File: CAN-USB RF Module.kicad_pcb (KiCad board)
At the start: 4 copper layers, 115 parts, among them IC1 ESDALC6V1W5, J1 USB JMPR, J2 USB_B_Micro, J3 Conn_Coaxial, J4 Conn_01x02_Socket, J5 Conn_02x05_Top_Bottom, J6 Fuel Cell Connector, Q1 NMOS, Q2 NMOS, SW1 RESET, SW2 BOOT0, SW3 GPBTN, SW4 GPSW, U1 STM32L442KCU6, U4 FT234XD-R, U5 SX1276IMLTRT, U6 P4259-63, U7 MCP2542WFDxMF (CAN), U8 MAX14572, U9 TLV76601QWDRBRQ1, Y1 32MHz

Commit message: Done design
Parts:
- removed CR1: ESDCAN03-2BWY, footprints:SOT323-3L_STM
- removed J4: Conn_01x02_Socket, Connector_PinHeader_2.54mm:PinHeader_1x02_P2.54mm_Vertical
- removed R25, R29: 10k, Resistor_SMD:R_0402_1005Metric
- removed SW3: GPBTN, footprints:SMD_025816_WRE
- removed SW4: GPSW, Button_Switch_SMD:SW_SPDT_PCM12
- removed U7: MCP2542WFDxMF (CAN), Package_DFN_QFN:DFN-8-1EP_3x3mm_P0.65mm_EP1.55x2.4mm
- added C52: 1u, Capacitor_SMD:C_0603_1608Metric, F.Cu at (112.0, 105.7)
- added C53: 1u, Capacitor_SMD:C_0603_1608Metric, F.Cu at (116.7, 105.7)
- added C54: 10u, Capacitor_SMD:C_0603_1608Metric, F.Cu at (116.7, 104.1)
- added C55: 1u, Capacitor_SMD:C_0402_1005Metric, F.Cu at (149.7, 114.8)
- added C56: 22u, Capacitor_SMD:C_0603_1608Metric, F.Cu at (146.4, 115.1)
- added C57: 1u, Capacitor_SMD:C_0402_1005Metric, F.Cu at (147.7, 114.8)
- added C58: 1u, Capacitor_SMD:C_0402_1005Metric, F.Cu at (148.7, 114.8)
- added D11: BLUE, LED_SMD:LED_0603_1608Metric, F.Cu at (121.7, 101.5)
- added J7: Conn_01x09_Socket, Connector_Dsub:DSUB-9_Female_Horizontal_P2.77x2.84mm_EdgePinOffset7.70mm_Housed_MountingHolesOffset9.12mm, F.Cu at (138.8, 79.7)
- added R30: 600R, Resistor_SMD:R_0603_1608Metric, F.Cu at (121.7, 98.4)
- added U2: LP38690DTX, Package_TO_SOT_SMD:TO-252-3_TabPin2, F.Cu at (113.5, 112.9)
- added U3: MCP2542FDxMF, Package_DFN_QFN:DFN-8-1EP_3x3mm_P0.65mm_EP1.55x2.4mm, F.Cu at (138.7, 87.9)
- J2: footprint Connector_USB:USB_Micro-B_Amphenol_10118194_Horizontal -> footprints:USB_Micro-B_Amphenol_10118194_Horizontal; moved to F.Cu
- J3: footprint Connector_Coaxial:SMA_Amphenol_132289_EdgeMount -> footprints:TAOGLAS_EMPCB.SMAFSTJ.B.HT
- J6: footprint Connector_Molex:Molex_Micro-Fit_3.0_43045-0621_2x03-1MP_P3.00mm_Horizontal -> footprints:Molex_Micro-Fit_3.0_43045-0621_2x03-1MP_P3.00mm_Horizontal
- RV1: footprint Potentiometer_THT:Potentiometer_Bourns_3386P_Vertical -> footprints:Potentiometer_Bourns_3386P_Vertical
- moved J6 120.4 mm to (104.9, 81.2)
- moved D1 117.1 mm to (189.1, 76.1)
- moved J5 112.9 mm to (183.6, 75.4), turned to -90 degrees
- moved J2 112.0 mm to (122.2, 73.9), turned to 180 degrees
- moved C40 111.6 mm to (141.5, 86.2)
- moved JP2 108.7 mm to (113.2, 84.1), turned to -90 degrees
- moved IC1 107.5 mm to (169.8, 76.8), turned to 180 degrees
- moved C13 106.5 mm to (125.4, 80.1), turned to 180 degrees
- moved R11 104.6 mm to (111.2, 86.9), turned to 180 degrees
- moved C39 104.0 mm to (138.9, 90.9), turned to 90 degrees
- moved R22 102.4 mm to (109.5, 88.4), turned to 180 degrees
- moved D5 101.4 mm to (114.1, 89.7), turned to -90 degrees
- moved D3 100.1 mm to (122.6, 80.0), turned to 0 degrees
- moved R10 99.6 mm to (110.7, 90.4), turned to 180 degrees
- moved R19 97.6 mm to (113.3, 91.9), turned to 0 degrees
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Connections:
- net Net-(U5-PA_BOOST) renamed /LoRa Tranciever/RFO_HF
- U1 pad 2: Net-(U1-PC14) -> /DIO5
- U1 pad 25: Net-(U1-PA15) -> /DIO4
- U5 pad 12: /DIO3 -> /DIO4
- U5 pad 13: /DIO3 -> /DIO5
- U8 pad 15: (no net) -> GND
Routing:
- net +3V3: track 25.3 -> 318.9 mm, vias 5 -> 20
- net /SW_RXTX: track 0.00 -> 77.1 mm, vias 0 -> 4
- net +5V: track 3.97 -> 69.4 mm, vias 0 -> 4
- net /DEBUG_SWDIO: track 18.5 -> 68.7 mm
- net /DEBUG_SWCLK: track 22.4 -> 66.9 mm, vias 2 -> 4
- net /DEBUG_SWO: track 23.9 -> 63.9 mm
- net VBUS_UP: track 52.4 -> 14.6 mm, vias 3 -> 1
- net /DIO5: track 0.00 -> 36.4 mm, vias 0 -> 4
- net /LoRa Tranciever/RXTX_SX: track 0.00 -> 32.0 mm, vias 0 -> 2
- net Net-(U1-PA15): track 31.0 -> 0.00 mm, vias 2 -> 0
- net /DIO3: track 0.00 -> 30.4 mm, vias 0 -> 2
- net /SPI1_NSS: track 0.00 -> 28.6 mm
- net /CAN_RX: track 43.0 -> 15.0 mm
- net /DIO2: track 0.00 -> 27.1 mm, vias 0 -> 2
- net /SX_RESET: track 0.00 -> 26.1 mm, vias 0 -> 2
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- added copper zone on F.Cu, net +12V
- added copper zone on In2.Cu, net +5V
- added copper zone on F.Cu, net /Power Regulator/12V
- added copper zone on B.Cu, net GND
- added copper zone on F.Cu, net GND
- added copper zone on In1.Cu, net GND
- removed copper zone on F.Cu, net +5V
- removed copper zone on In2.Cu, net VBUS_UP
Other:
- board outline added: 95 x 47.2 mm
- board text added: "Horizontal Top Layer Vertical Bottom layer"
- board text added: "RESET"
- board text added: "USB RX/TX"
- board text removed: "RX/TX"

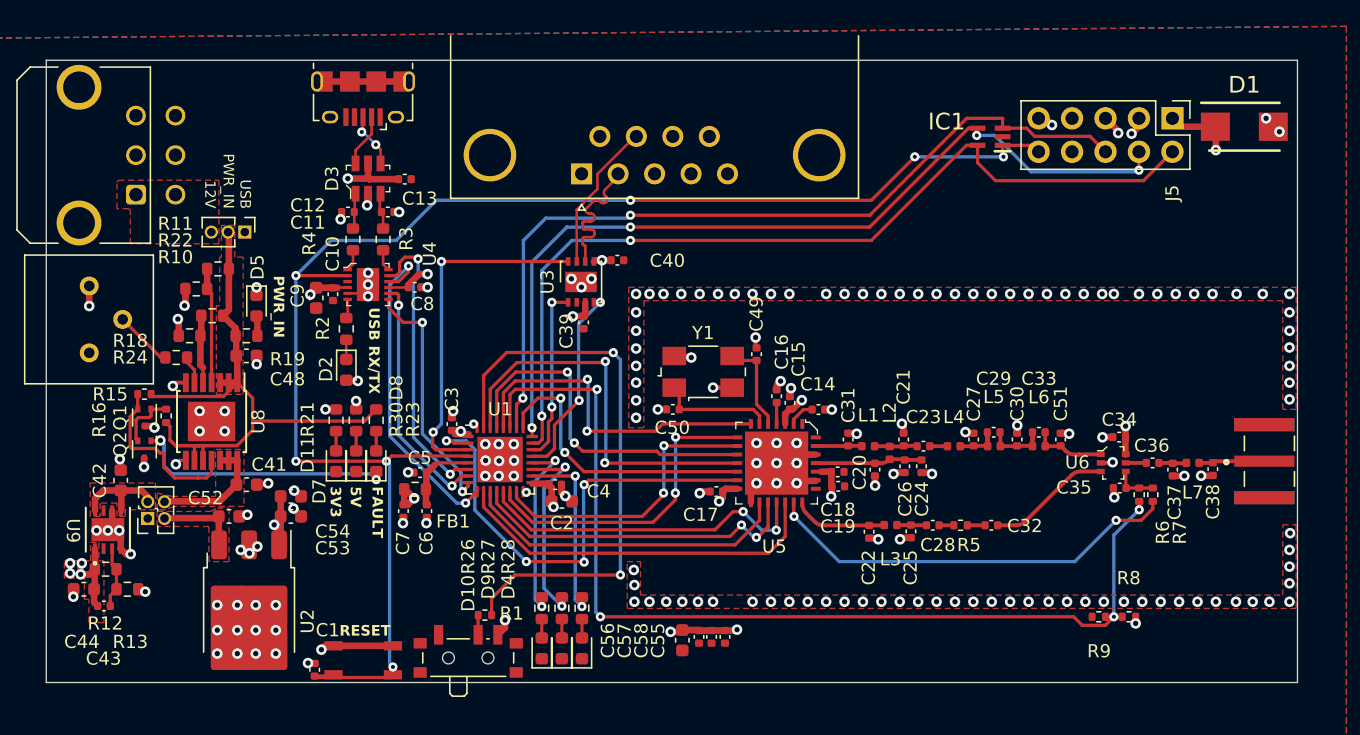
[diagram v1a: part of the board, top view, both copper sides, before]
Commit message: Added stiching vias
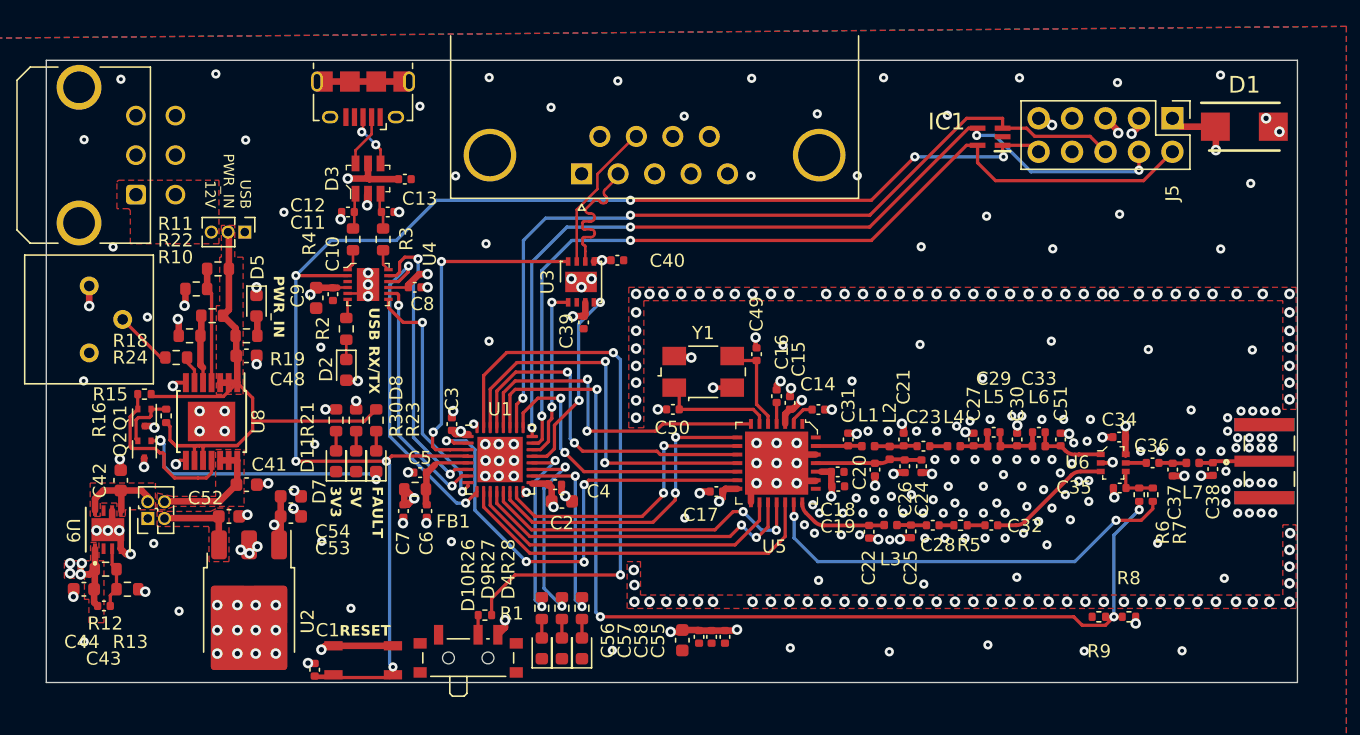
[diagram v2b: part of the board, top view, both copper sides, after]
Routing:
- net /LoRa Tranciever/RXTX_SX: track 32.0 -> 32.9 mm
- net +3V3: track 318.9 -> 319.7 mm
- net GND: vias 194 -> 349

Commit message: a
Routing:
- net VBUS_UP: track 14.6 -> 24.5 mm, vias 1 -> 3
- net /SPI1_NSS: track 28.6 -> 29.8 mm
- net /SPI1_SCK: track 24.9 -> 25.8 mm
- net /SPI1_MISO: track 25.5 -> 26.2 mm
- net /DIO5: track 36.4 -> 37.0 mm
- net GND: vias 349 -> 389
- added copper zone on In2.Cu, net VBUS_UP

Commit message: Done
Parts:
- removed C52, C53: 1u, Capacitor_SMD:C_0603_1608Metric
- removed R12: 500k, Resistor_SMD:R_0603_1608Metric
- removed R13: 160k, Resistor_SMD:R_0603_1608Metric
- removed U9: TLV76601QWDRBRQ1, footprints:TLV76601QWDRBRQ1_TEX
- added U7: AZ1117-3.3, Package_TO_SOT_SMD:SOT-223-3_TabPin2, F.Cu at (107.3, 112.4)
- C42: value 1u -> 10u
- C43: value 10p -> 10u; footprint Capacitor_SMD:C_0402_1005Metric -> Capacitor_SMD:C_0603_1608Metric
- C44: value 2u2 -> 22u
- C54: value 10u -> 22u
- J1: footprint Connector_PinHeader_1.27mm:PinHeader_2x02_P1.27mm_Vertical -> Connector_PinHeader_2.54mm:PinHeader_2x02_P2.54mm_Vertical
- JP2: footprint Connector_PinHeader_1.27mm:PinHeader_1x03_P1.27mm_Vertical -> Connector_PinHeader_2.54mm:PinHeader_1x03_P2.54mm_Vertical
- U2: value LP38690DTX -> AZ1117-5.0; footprint Package_TO_SOT_SMD:TO-252-3_TabPin2 -> Package_TO_SOT_SMD:SOT-223-3_TabPin2
- moved C42 14.0 mm to (104.9, 116.8), turned to 0 degrees
- moved C43 13.6 mm to (114.0, 105.2)
- moved C54 11.7 mm to (116.3, 115.8)
- moved U2 3.24 mm to (115.7, 110.5)
- moved J1 1.86 mm to (107.4, 106.9)
- moved JP2 1.35 mm to (114.5, 84.3)
- moved R22 1.32 mm to (110.7, 88.9)
- moved C44 1.16 mm to (102.1, 111.5), turned to 90 degrees
- moved R10 1.03 mm to (111.8, 90.4)
- moved R18 0.96 mm to (110.0, 91.9)
- moved R11 0.77 mm to (111.8, 87.4)
- moved C49 0.17 mm to (151.9, 93.3)
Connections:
- C43 pad 1: +3V3 -> /Power Regulator/12V
- C43 pad 2: /Power Regulator/FB -> GND
- U2 pad 1: +5V -> GND
- U2 pad 2: GND -> +5V
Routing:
- net GND: track 69.5 -> 57.4 mm, vias 389 -> 361
- net +3V3: track 319.7 -> 309.6 mm, vias 20 -> 19
- net /Power Regulator/5V: track 7.30 -> 15.7 mm, vias 0 -> 1
- net /Power Regulator/FB: track 4.68 -> 0.00 mm
- net +5V: track 69.4 -> 73.8 mm
- net /CAN Tranciever/CD-: track 11.3 -> 7.69 mm
- net /Power Regulator/FUSE_OUT: track 9.14 -> 6.23 mm
- net VBUS_UP: track 24.5 -> 26.1 mm, vias 3 -> 2
- net Net-(R24-Pad2): track 4.44 -> 5.58 mm
- net /DEBUG_SWO: track 64.0 -> 63.4 mm
- net /Power Regulator/FUSE_IN: track 50.3 -> 49.7 mm
- added copper zone on In2.Cu, net +3V3
- added copper zone on F.Cu, net +5V
- added copper zone on In2.Cu, net /Power Regulator/5V
- removed copper zone on F.Cu, net +12V
- removed copper zone on In2.Cu, net +5V
- removed copper zone on F.Cu, net /Power Regulator/5V

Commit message: Added logo and assigned parts
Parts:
- removed the Q1 at (105.6, 98.2)
- removed the R16 at (107.2, 98.0)
- added G***: LOGO, LOGO, B.Cu at (178.9, 116.5)
- added H1: MountingHole, MountingHole:MountingHole_2.2mm_M2, F.Cu at (189.7, 73.9)
- added H2: MountingHole, MountingHole:MountingHole_2.2mm_M2, F.Cu at (189.9, 115.6)
- added H3: MountingHole, MountingHole:MountingHole_2.2mm_M2, F.Cu at (114.6, 74.2)
- added H4: MountingHole, MountingHole:MountingHole_2.2mm_M2, F.Cu at (114.7, 115.6)
- added U9: Common Cathode SBD, Package_TO_SOT_SMD:SOT-23, F.Cu at (116.5, 79.5)
- C2: footprint Capacitor_SMD:C_0603_1608Metric -> Capacitor_SMD:C_0805_2012Metric
- D10: renamed from D2; value AMBER RX/TX -> AMBER
- SW2: renamed from SW1; footprint footprints:SMD_025816_WRE -> Button_Switch_SMD:SW_SPST_PTS810
- Y1: footprint Crystal:Crystal_SMD_0603-4Pin_6.0x3.5mm -> Crystal:Crystal_SMD_2016-4Pin_2.0x1.6mm
- moved C13 10.0 mm to (123.4, 108.6), turned to -90 degrees
- moved Q1 9.00 mm to (114.6, 101.3)
- moved R15 8.46 mm to (114.0, 96.5), turned to -90 degrees
- moved C11 6.82 mm to (112.9, 109.9), turned to -90 degrees
- moved D4 4.42 mm to (187.7, 80.3), turned to -90 degrees
- moved C21 3.26 mm to (149.0, 97.7)
- moved U4 2.74 mm to (118.2, 109.3), turned to 180 degrees
- moved Y1 2.43 mm to (150.2, 95.8)
- moved C20 1.55 mm to (152.1, 94.9)
- moved C2 0.97 mm to (138.2, 104.9)
- moved SW2 0.25 mm to (122.2, 116.3)
- moved C1 0.13 mm to (118.6, 117.2)
- renumbered C42 to C10, C54 to C11, C41 to C12, C43 to C13, C8 to C14, C9 to C15, C10 to C16, C11 to C17, C12 to C18, C13 to C19, C49 to C20, C50 to C21, C14 to C22, C15 to C23, C16 to C24, C17 to C25, C18 to C26, C19 to C27, C31 to C28, C20 to C29, C21 to C30, C23 to C31, C22 to C32, C24 to C33, C26 to C34, C25 to C35, C27 to C36, C55 to C37, C28 to C38, C29 to C39, C30 to C40, C33 to C41, C32 to C42, C51 to C43, C56 to C44, C34 to C45, C57 to C46, C35 to C47, C58 to C48, C36 to C49, C37 to C50, C38 to C51, C39 to C52, C40 to C53, C44 to C8, C48 to C9, D10 to D1, D3 to D11, D9 to D2, D4 to D3, D1 to D4, D7 to D6, D11 to D7, D8 to D9, J5 to J1, J1 to J2, J6 to J3, J2 to J4, J3 to J5, J7 to J6, JP2 to JP1, Q2 to Q1, R18 to R10, R22 to R12, R24 to R13, R30 to R14, R23 to R16, R2 to R17, R3 to R18, R4 to R19, R1 to R2, R5 to R20, R6 to R21, R7 to R22, R8 to R23, R9 to R24, R26 to R4, R27 to R5, R28 to R6, R19 to R7, R21 to R8, R10 to R9, SW2 to SW3, U7 to U2, U8 to U3, U2 to U4, U4 to U5, U5 to U6, U6 to U7, U3 to U8
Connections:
- J3 pad 3: unconnected-(J6-Pin_3-Pad3) (its old number) -> /Power Regulator/5V_UP
- J3 pad 6: unconnected-(J6-Pin_6-Pad6) (its old number) -> /Power Regulator/5V_UP
- Q1 pad 2: Net-(Q1-D) -> /Power Regulator/~{FLAG}
- R15 pad 1: /Power Regulator/FUSE_IN -> Net-(R15-Pad1)
- R16 pad 1: /Power Regulator/FUSE_IN -> Net-(R15-Pad1)
- SW2 pad 2: GND -> /NRST
- U3 pad 10: /Power Regulator/FUSE_IN -> GND
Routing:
- net /Power Regulator/FUSE_IN: track 49.7 -> 22.3 mm
- net Net-(R15-Pad1): track 0.00 -> 26.9 mm
- net /Power Regulator/5V_UP: track 0.00 -> 12.4 mm
- net Net-(D9-K): track 19.9 -> 10.1 mm, vias 2 -> 0
- net VBUS_UP: track 26.1 -> 35.4 mm
- net /Power Regulator/12V: track 5.97 -> 14.5 mm
- net Net-(Q1-D): track 4.59 -> 0.00 mm
- net /Power Regulator/~{FLAG}: track 13.0 -> 8.39 mm
- net Net-(U6-XTB): track 8.73 -> 5.04 mm
- net +3V3: track 309.6 -> 307.2 mm
- net Net-(U6-XTA): track 7.06 -> 5.00 mm
- net /NRST: track 116.4 -> 114.7 mm
- net /DIO1: track 22.3 -> 23.5 mm
- net /SPI1_SCK: track 25.8 -> 26.8 mm
- net /DIO0: track 24.4 -> 25.3 mm
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- added copper zone on F.Cu, net +12V
- removed copper zone on In2.Cu, net +3V3
- removed copper zone on F.Cu, net /Power Regulator/12V
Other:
- board text added: "Telemetry Module Rev 1.0"
- board text added: "~{FAULT}"
- board text removed: "EcoCar Telemetry Module Rev 1.0"
- board text removed: "FAULT"

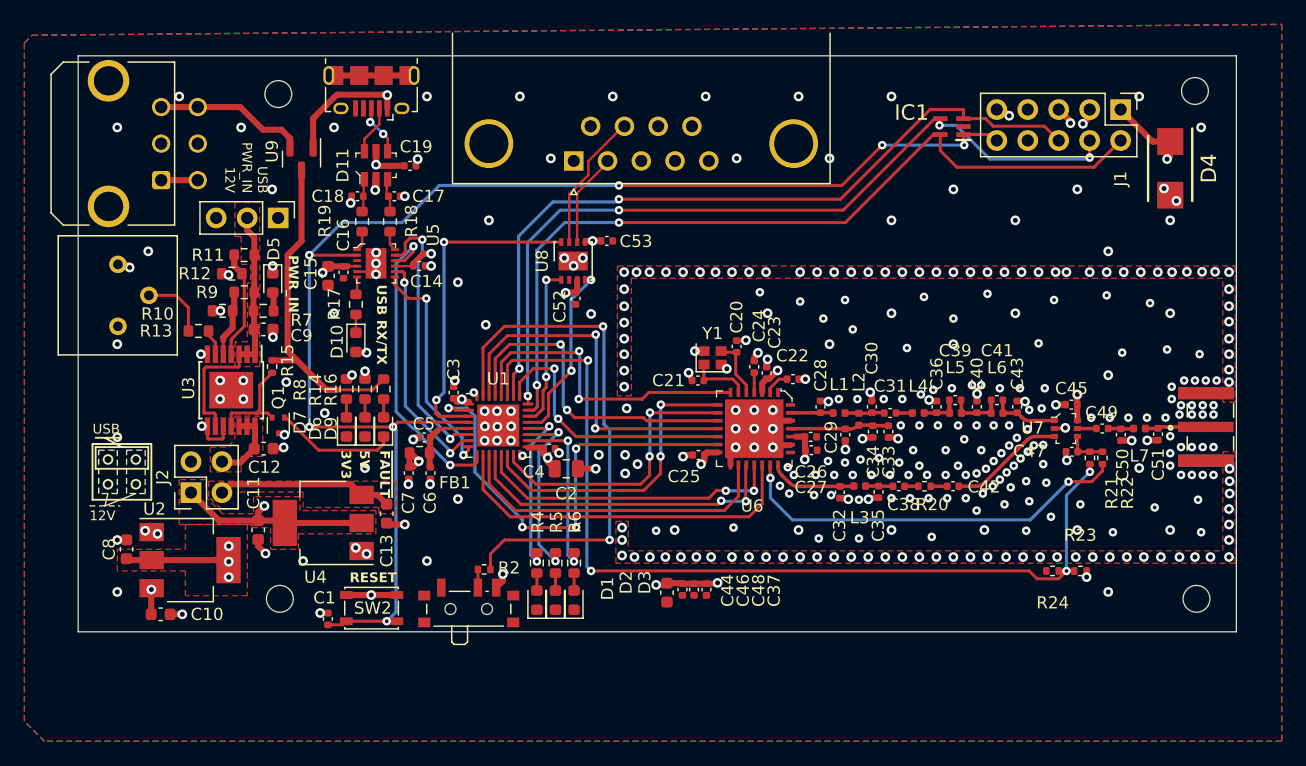
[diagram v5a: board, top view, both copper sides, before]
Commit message: Ready to order added all part numbers
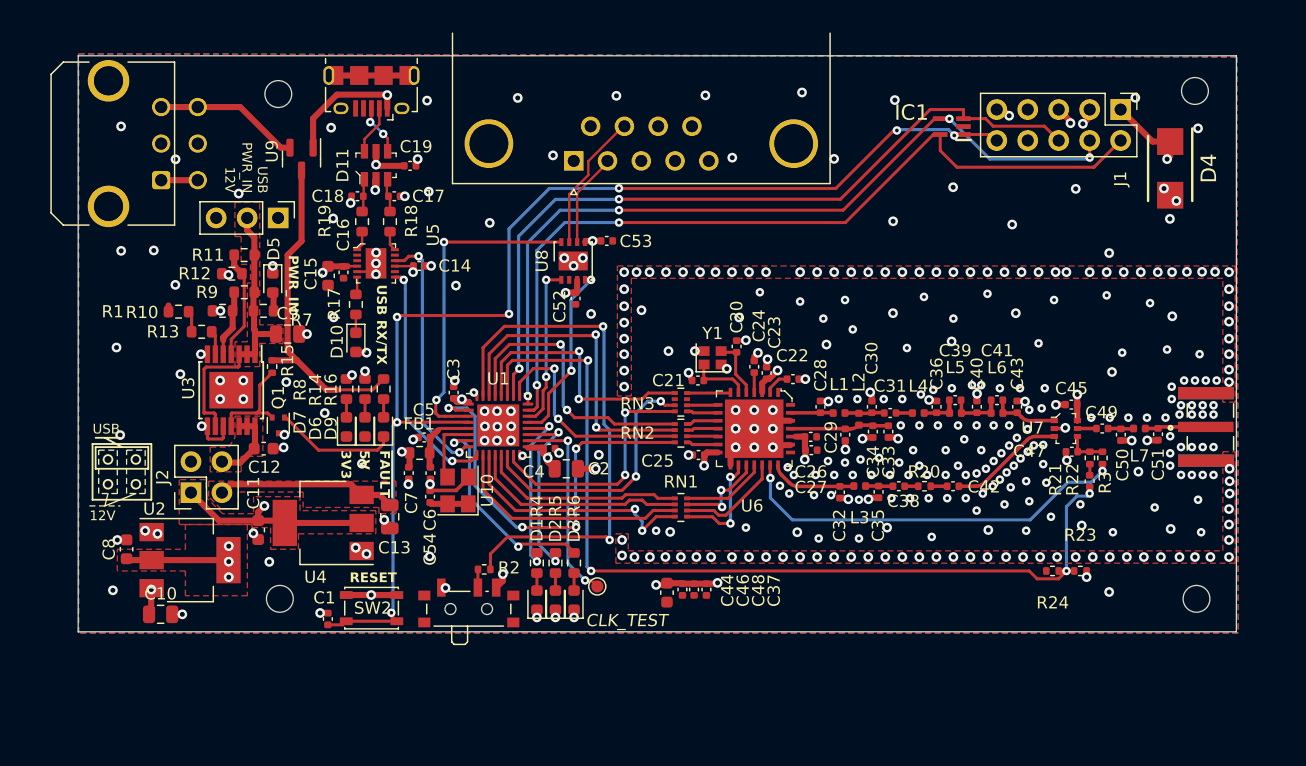
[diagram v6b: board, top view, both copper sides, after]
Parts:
- removed RV1: SETI, footprints:Potentiometer_Bourns_3386P_Vertical
- added C54: u1, Capacitor_SMD:C_0402_1005Metric, F.Cu at (127.0, 107.2)
- added R1: 1k5, Resistor_SMD:R_0603_1608Metric, F.Cu at (106.4, 92.0)
- added R3: 100R, Capacitor_SMD:C_0402_1005Metric, F.Cu at (181.1, 105.9)
- added RN1: 100R, Resistor_SMD:R_Array_Concave_4x0402, F.Cu at (147.6, 108.1)
- added RN2: 100R, Resistor_SMD:R_Array_Concave_4x0402, F.Cu at (147.6, 102.0)
- added RN3: 100R, Resistor_SMD:R_Array_Concave_4x0402, F.Cu at (147.6, 99.4)
- added TP1: CLK_TEST, TestPoint:TestPoint_Pad_D1.0mm, F.Cu at (140.7, 114.6)
- added U10: 8MHz, Crystal:Crystal_SMD_3225-4Pin_3.2x2.5mm, F.Cu at (129.3, 106.7)
- C10, C13, C9: footprint Capacitor_SMD:C_0603_1608Metric -> Capacitor_SMD:C_0805_2012Metric
- R4, R5, R6: value 10k -> 110R
- moved G*** 31.2 mm to (186.1, 86.1)
- moved C9 2.01 mm to (115.3, 93.9)
- moved C13 0.36 mm to (123.7, 108.8)
- moved R13 0.27 mm to (108.3, 93.7)
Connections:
- R21 pad 2: /SW_RXTX -> /LoRa Tranciever/RXTX_EXT
- R23 pad 1: /SW_RXTX -> /LoRa Tranciever/RXTX_EXT
- R24 pad 2: /SW_RXTX -> /LoRa Tranciever/RXTX_EXT
- R6 pad 2: Net-(U1-PA8) -> Net-(U1-PA1)
- U1 pad 6: /UART2_USB_CTS -> /XCLK
- U1 pad 7: /UART2_USB_RTS -> Net-(U1-PA1)
- U5 pad 10: /UART2_USB_RX -> /UART2_USB_TX
- U5 pad 11: /UART2_USB_CTS -> /USB Interface/CTS
- U5 pad 2: /NRST -> /USB Interface/RESET
- U5 pad 7: /UART2_USB_TX -> /UART2_USB_RX
- U5 pad 8: /UART2_USB_RTS -> /USB Interface/RTS
- U6 pad 10: /DIO2 -> /LoRa Tranciever/DIO2
- U6 pad 11: /DIO3 -> /LoRa Tranciever/DIO3
- U6 pad 12: /DIO4 -> /LoRa Tranciever/DIO4
- U6 pad 13: /DIO5 -> /LoRa Tranciever/DIO5
- U6 pad 16: /SPI1_SCK -> /LoRa Tranciever/SCK_RTSN
- U6 pad 17: /SPI1_MISO -> /LoRa Tranciever/MISO_TX
- U6 pad 18: /SPI1_MOSI -> /LoRa Tranciever/MOSI_RX
- U6 pad 19: /SPI1_NSS -> /LoRa Tranciever/NSS_CTS
- U6 pad 7: /SX_RESET -> /LoRa Tranciever/SX1276_NRESET
- U6 pad 8: /DIO0 -> /LoRa Tranciever/DIO0
- U6 pad 9: /DIO1 -> /LoRa Tranciever/DIO1
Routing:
- net /UART2_USB_CTS: track 22.6 -> 0.00 mm, vias 2 -> 0
- net /UART2_USB_RTS: track 19.1 -> 0.00 mm, vias 2 -> 0
- net /NRST: track 114.7 -> 97.1 mm
- net Net-(U1-PA1): track 0.00 -> 17.6 mm, vias 0 -> 2
- net /SPI1_NSS: track 30.3 -> 19.8 mm
- net /LoRa Tranciever/SCK_RTSN: track 0.00 -> 9.05 mm, vias 0 -> 2
- net /LoRa Tranciever/NSS_CTS: track 0.00 -> 8.70 mm
- net /SPI1_MISO: track 26.5 -> 17.8 mm, vias 2 -> 0
- net /SPI1_MOSI: track 25.4 -> 16.8 mm, vias 2 -> 0
- net /LoRa Tranciever/MISO_TX: track 0.00 -> 7.67 mm, vias 0 -> 2
- net /LoRa Tranciever/MOSI_RX: track 0.00 -> 7.01 mm
- net /SPI1_SCK: track 26.8 -> 20.5 mm, vias 0 -> 2
- net GND: track 58.1 -> 64.2 mm, vias 375 -> 377
- net /UART2_USB_RX: track 25.6 -> 19.7 mm
- net /XCLK: track 0.00 -> 5.32 mm
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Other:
- board text added: "Telemetry Module ${REVISION} ${ISSUE_DATE} ${COMMENT1}"
- board text removed: "Telemetry Module Rev 1.0"
